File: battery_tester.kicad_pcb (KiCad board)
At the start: 2 copper layers, 130 x 100 mm, 132 parts, among them IC1 IP5506, IC2 LM3940IMP-3.3, J1 Conn_BAL, J10 Conn_01x02_Pin, J11 USB-C_12pin, J12 Conn_01x07_Pin, J13 MicroSD_Connector_503182-1852, J2 Conn_BAT, J3 Screw_Terminal_01x02, J4 Screw_Terminal_01x02, J6 CON05, J7 CON05, J9 Conn_01x02_Pin, M1 OLED12864-I2C, Q1 IRF8721PBF-1, U1 STM32G484RETx, U2 ACS713xLCTR-30A, U3 BTS7004-1EPP, U4 BTS7004-1EPP, U6 TMP101, X1 ASCO, X2 ASAK

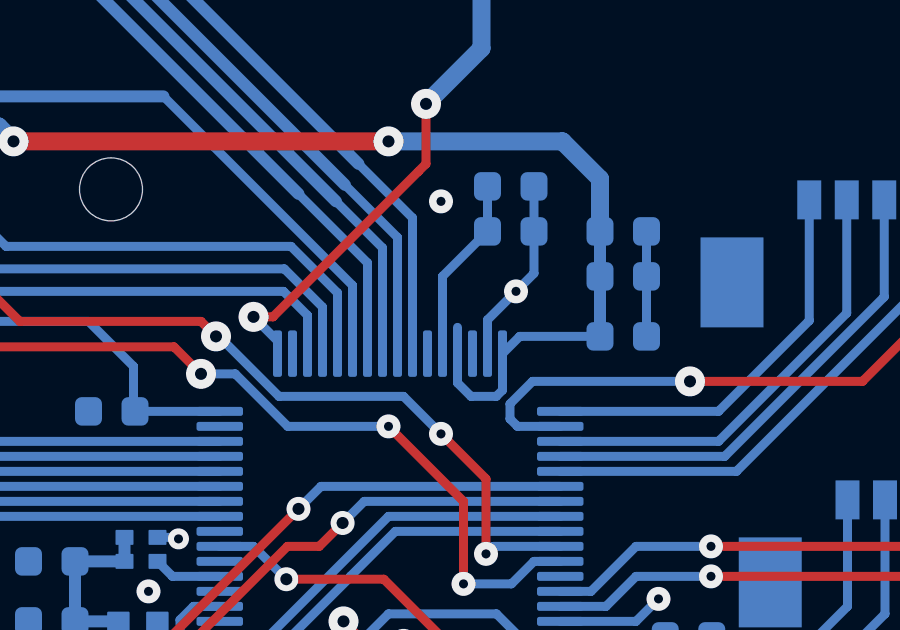
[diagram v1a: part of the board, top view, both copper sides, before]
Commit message: Add missing VRef connection to 3V3.
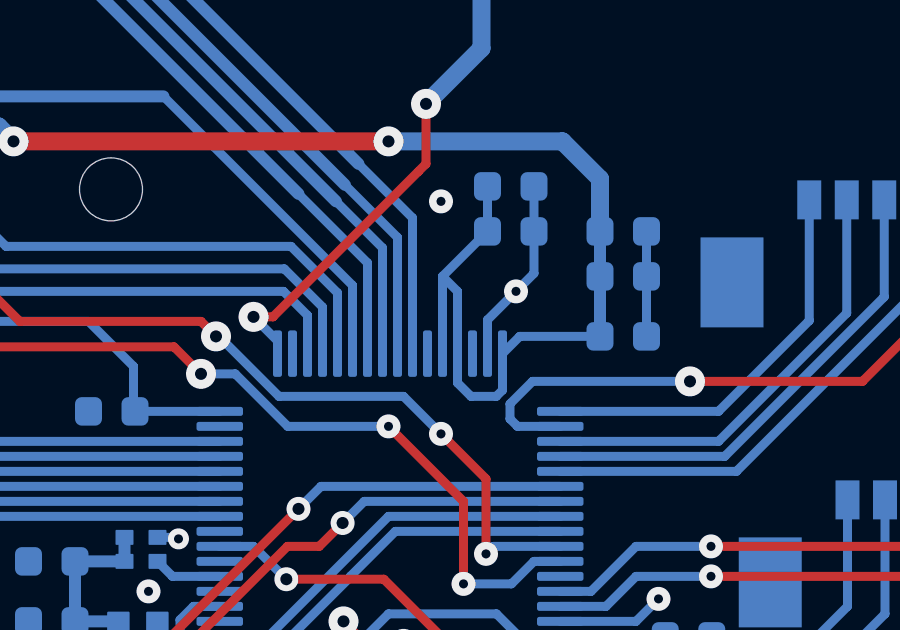
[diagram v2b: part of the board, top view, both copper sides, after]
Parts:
- R10, R11, R12, R13, R15, R16: value R -> 10k
- R4: value R -> 68k
- R5: value R -> 56k
- R6: value R -> 47k
- R7: value R -> 33k
- R8: value R -> 18k
- R9: value R -> 3.3k
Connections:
- C25 pad 1: Net-(U1-VREF+) -> +3.3V
- C26 pad 1: Net-(U1-VREF+) -> +3.3V
- U1 pad 28: Net-(U1-VREF+) -> +3.3V
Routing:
- net +3.3V: track 325.1 -> 333.3 mm
- net Net-(U1-VREF+): track 6.20 -> 0.00 mm
